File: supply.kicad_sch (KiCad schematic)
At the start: 25 parts, among them Q4 2N7002K, Q5 BSS83P, SW202 PWR_ON, U2 TPS630701RNMR

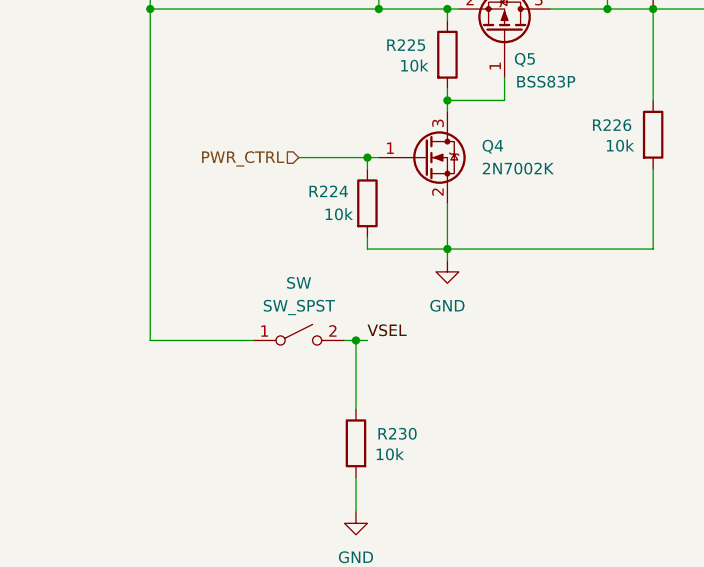
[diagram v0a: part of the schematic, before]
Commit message: Solder jumpers for smaller simpler supply
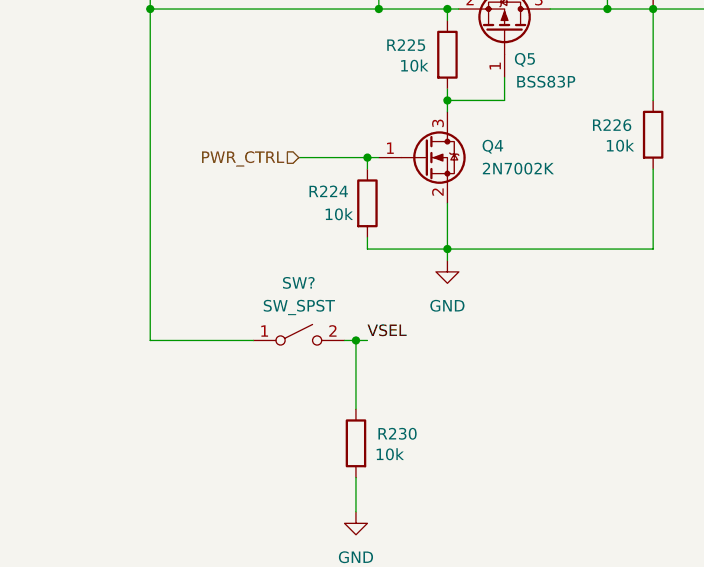
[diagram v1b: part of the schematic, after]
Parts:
- renumbered SW to SW?
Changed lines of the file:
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@@
 		(dnp no)
 		(fields_autoplaced yes)
-		(property "Reference" "SW"
+		(property "Reference" "SW?"
 			(at 60.96 153.67 0)
 			(effects
@@
 		(instances
 			(project "BreadboardUPS"
+				(path "/3f1ccd97-6ac6-4e7a-a00a-840cd07719d8/18807fed-8172-4214-972d-ede11085980e"
+					(reference "SW?")
+					(unit 1)
+				)
 				(path "/3f1ccd97-6ac6-4e7a-a00a-840cd07719d8/4649fa7b-adfb-4d4b-ad62-a47049ee155c"
 					(reference "SW1")

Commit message: Part selection
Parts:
- removed C3: 1u, Capacitor_SMD:C_1206_3216Metric_Pad1.33x1.80mm_HandSolder, symbol Device:C
- removed L1: 1.5u, Inductor_SMD_Wurth:L_Wurth_WE-LQSH-2512, symbol Device:L
- removed R2: 220k, Resistor_SMD:R_1206_3216Metric_Pad1.30x1.75mm_HandSolder, symbol Device:R
- removed R3: 470k, Resistor_SMD:R_1206_3216Metric_Pad1.30x1.75mm_HandSolder, symbol Device:R
- removed R4: 150k, Resistor_SMD:R_1206_3216Metric_Pad1.30x1.75mm_HandSolder, symbol Device:R
- removed SW?: SW_SPST, symbol Switch:SW_SPST
- removed U2: TPS630701RNMR, lib:TPS63070, symbol TPS63070:TPS630701RNMR
- added C408: 1u, Capacitor_SMD:C_0805_2012Metric_Pad1.18x1.45mm_HandSolder, symbol Device:C
- added JP401: SolderJumper_2_Open, Jumper:SolderJumper-2_P1.3mm_Open_RoundedPad1.0x1.5mm, symbol Jumper:SolderJumper_2_Open
- added L401: 1.5u, Inductor_SMD:L_Cenker_CKCS4020, symbol Device:L
- added R410: 220k, Resistor_SMD:R_0805_2012Metric_Pad1.20x1.40mm_HandSolder, symbol Device:R
- added R411: 470k, Resistor_SMD:R_0805_2012Metric_Pad1.20x1.40mm_HandSolder, symbol Device:R
- added R412: 150k, Resistor_SMD:R_0805_2012Metric_Pad1.20x1.40mm_HandSolder, symbol Device:R
- added SW401: Vsel, Button_Switch_THT:SW_Slide_SPDT_Straight_CK_OS102011MS2Q, symbol Switch:SW_SPDT
- added TP401: VSEL, TestPoint:TestPoint_Pad_D2.0mm, symbol Connector:TestPoint
- added U401: TPS630701RNMR, lib:TPS63070, symbol TPS63070:TPS630701RNMR
- C401: renamed from C1; now left out of the parts list
- C402: renamed from C2; now left out of the parts list
- C404: renamed from C4; now left out of the parts list
- C405: renamed from C5; now left out of the parts list
- C406: renamed from C6; now left out of the parts list
- C407: renamed from C7; now left out of the parts list
- Q401: renamed from Q4; value 2N7002K -> DO2308S; footprint Package_TO_SOT_SMD:SOT-23 -> Package_TO_SOT_SMD:SOT-23_Handsoldering; LCSC (none) -> C47018572
- Q402: renamed from Q5; value BSS83P -> DO2309A; footprint Package_TO_SOT_SMD:SOT-23 -> Package_TO_SOT_SMD:SOT-23_Handsoldering; LCSC (none) -> C47018570
- R401: renamed from R230; now left out of the parts list
- R402: renamed from R224; now left out of the parts list
- R403: renamed from R225; now left out of the parts list
- R404: renamed from R1; now left out of the parts list
- R405: renamed from R226; now left out of the parts list
- R409: renamed from R5; now left out of the parts list
- SW402: renamed from SW202; footprint Button_Switch_SMD:SW_SPST_PTS647_Sx38 -> Button_Switch_THT:SW_PUSH_6mm; now left out of the parts list
- TP402: renamed from TP12; footprint TestPoint:TestPoint_Pad_D1.0mm -> TestPoint:TestPoint_Pad_D2.0mm; now left out of the parts list
- TP403: renamed from TP6; footprint TestPoint:TestPoint_Pad_D1.0mm -> TestPoint:TestPoint_Pad_D2.0mm; now left out of the parts list
- TP404: renamed from TP7; footprint TestPoint:TestPoint_Pad_D1.0mm -> TestPoint:TestPoint_Pad_D2.0mm; now left out of the parts list
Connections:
- net EN: now also JP401.2 (B), U401.14 (EN)
- net GND: now also C408.2, R412.2, SW401.1 (A), U401.10 (PGND), U401.4 (GND); no longer R401.2
- net VSEL: now also R401.2, SW401.2 (B), TP401.1, U401.15 (VSEL); no longer R401.1
- net Vin: now also R401.1, C408.1, JP401.1 (A), U401.12 (VIN), U401.13 (VIN)
- net Vout: now also R411.1, U401.7 (VOUT), U401.8 (VOUT)
- net at R409.2, TP403.1: now also U401.2 (PG)
- net at R404.2: now also U401.1 (PS_SYNC)
- net at C404.1: now also U401.3 (VAUX)
- new net: L401.1, U401.11 (L1)
- new net: R410.1, R411.2, R412.1, U401.5 (FB)
- new net: R410.2, U401.6 (FB2)
- new net: L401.2, U401.9 (L2)
- no-connect marks 0 -> 1
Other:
- moved on the sheet: R401

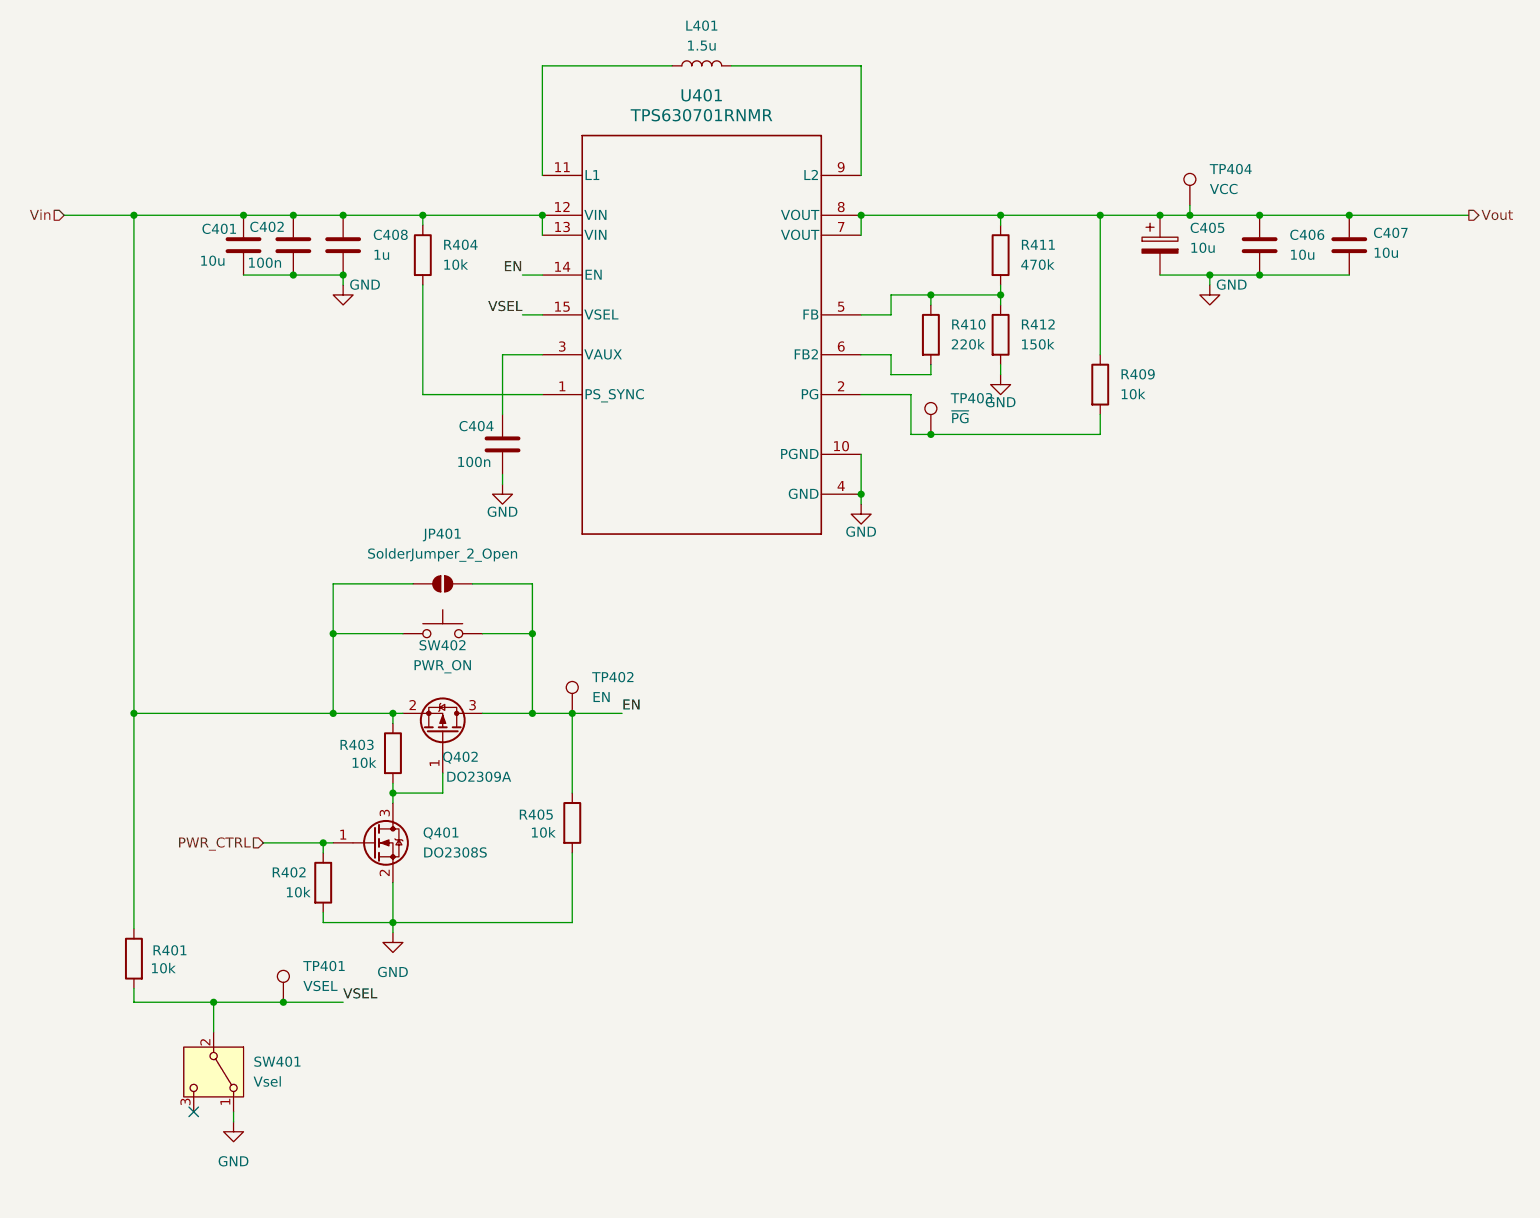
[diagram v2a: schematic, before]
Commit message: Add more LEDs
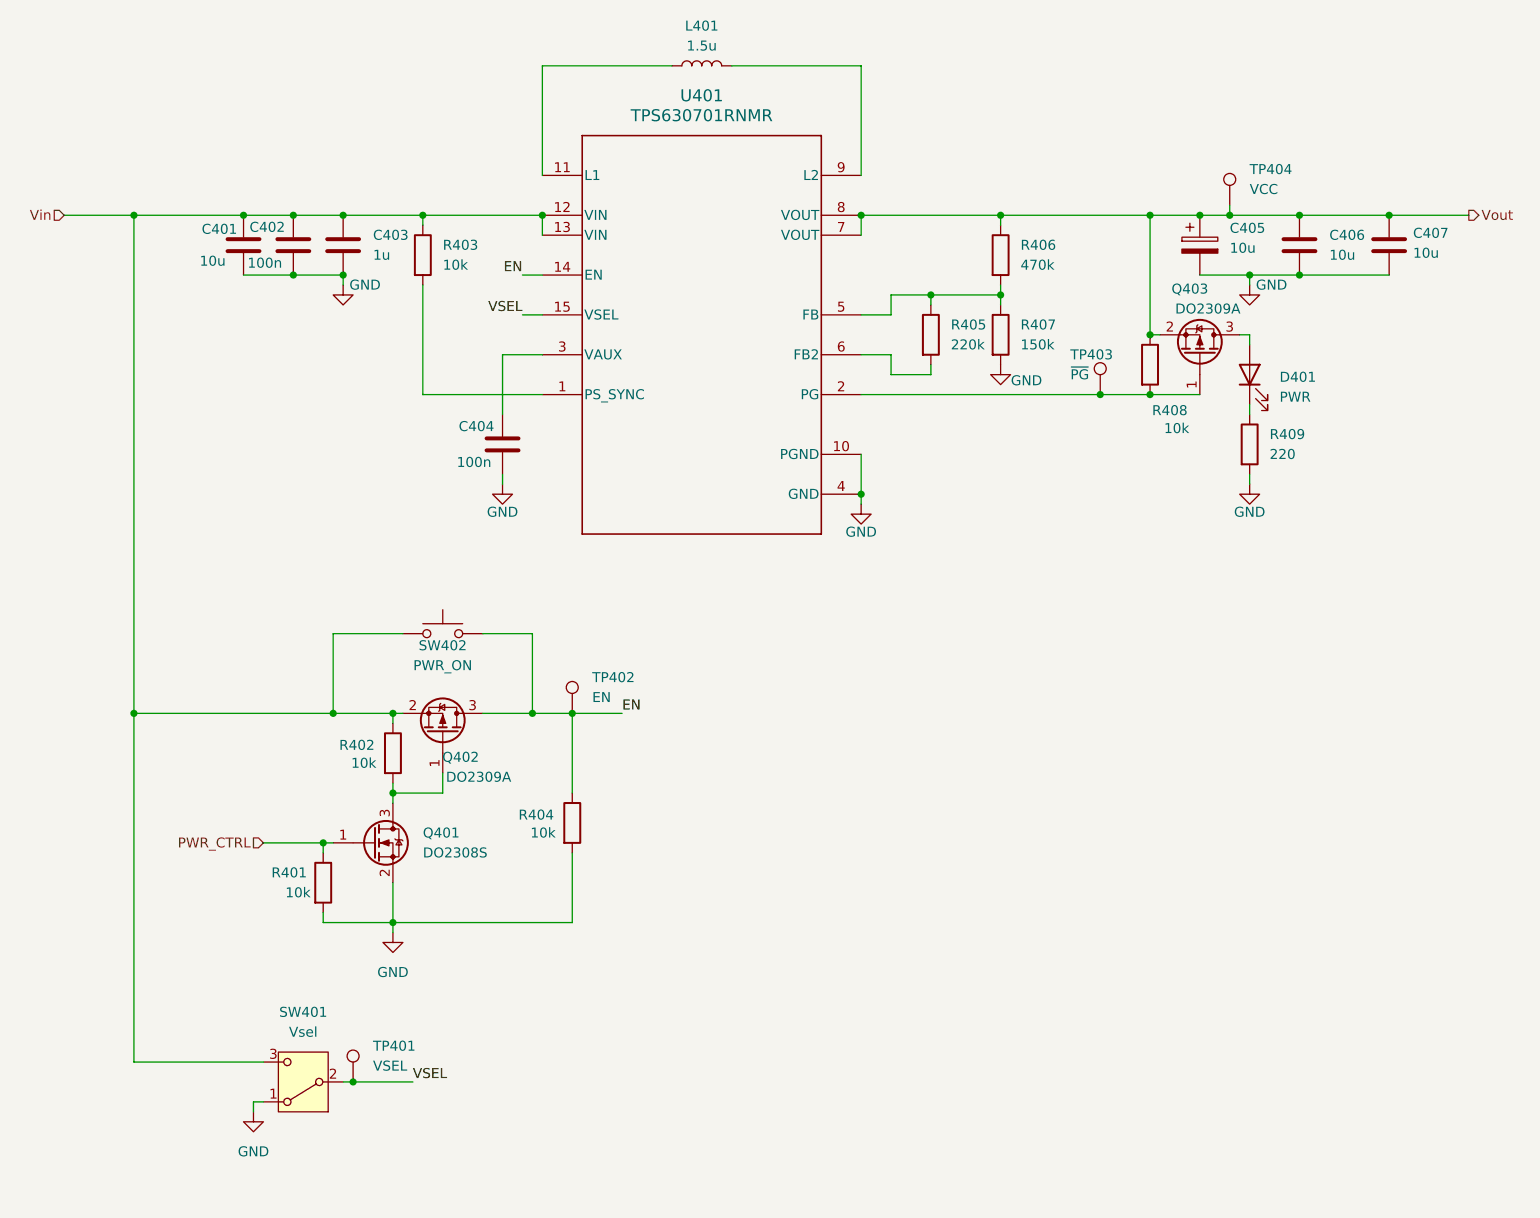
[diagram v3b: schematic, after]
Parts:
- removed JP401: SolderJumper_2_Open, Jumper:SolderJumper-2_P1.3mm_Open_RoundedPad1.0x1.5mm, symbol Jumper:SolderJumper_2_Open
- removed R401: 10k, Resistor_SMD:R_1206_3216Metric_Pad1.30x1.75mm_HandSolder, symbol Device:R
- added D401: PWR, LED_SMD:LED_1206_3216Metric_Pad1.42x1.75mm_HandSolder, symbol Device:LED
- added Q403: DO2309A, Package_TO_SOT_SMD:SOT-23_Handsoldering, symbol Transistor_FET:BSS83P
- added R408: 10k, Resistor_SMD:R_1206_3216Metric_Pad1.30x1.75mm_HandSolder, symbol Device:R
- R409: value 10k -> 220
- renumbered C408 to C403, R402 to R401, R403 to R402, R404 to R403, R405 to R404, R410 to R405, R411 to R406, R412 to R407
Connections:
- net GND: now also R409.2
- net Vin: now also SW401.3 (C)
- net Vout: now also Q403.2 (S), R408.1; no longer R409.1
- net at TP403.1, U401.2 (PG): now also Q403.1 (G), R408.2; no longer R409.2
- new net: D401.2 (A), Q403.3 (D)
- new net: D401.1 (K), R409.1
- no-connect marks 1 -> 0
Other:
- moved on the sheet: C405, C406, C407, SW401, TP401, TP403, TP404

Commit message: Connection naming
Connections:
- net PFM: now reaches R403.2, U401.1 (PS_SYNC)
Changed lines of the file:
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@@
+	)
+	(junction
+		(at 81.28 72.39)
+		(diameter 0)
+		(color 0 0 0 0)
 	)
 	(junction
@@
 	(wire
 		(pts
+			(xy 81.28 72.39) (xy 81.28 82.55)
+		)
+		(stroke
+			(width 0)
+			(type default)
+		)
+	)
+	(wire
+		(pts
 			(xy 81.28 59.69) (xy 81.28 60.96)
 		)
@@
 	(wire
 		(pts
-			(xy 81.28 68.58) (xy 81.28 82.55)
+			(xy 81.28 68.58) (xy 81.28 72.39)
 		)
 		(stroke
@@
 		(pts
 			(xy 68.58 140.97) (xy 68.58 139.7)
+		)
+		(stroke
+			(width 0)
+			(type default)
+		)
+	)
+	(wire
+		(pts
+			(xy 81.28 72.39) (xy 35.56 72.39)
 		)
 		(stroke
@@
 		)
 	)
+	(hierarchical_label "PFM"
+		(shape input)
+		(at 35.56 72.39 180)
+		(effects
+			(font
+				(size 1.27 1.27)
+			)
+			(justify right)
+		)
+	)
